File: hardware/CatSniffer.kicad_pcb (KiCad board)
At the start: 4 copper layers, 81 x 20 mm, 101 parts, among them J1 Antenna, J2 Conn_01x06_Female, J3 Conn_01x06_Female, P1 USB_C_Plug_USB2.0, SW1 SW, U1 AP2112K-3.3, U2 RFSW8006QTR7, U3 RP2040, U4 0900PC15A0036, U5 0900FM15D0039, U6 PE42421, U7 SX1262IMLTRT, U8 CC1352P1F3RGZT, U9 W25Q16JV, Y1 48MHz, Y2 32.768kHz, Y3 32Mhz, Y4 12MHz

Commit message: For revision
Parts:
- removed J2: Conn_01x06_Female, Connector:Tag-Connect_TC2030-IDC-NL_2x03_P1.27mm_Vertical
- moved R12 1.78 mm to (119.7, 109.9)
- moved G*** 1.17 mm to (130.3, 113.3)
- moved C39 0.72 mm to (116.0, 109.0), turned to 0 degrees
- moved C46 0.69 mm to (116.0, 110.0), turned to 0 degrees
- moved C28 0.54 mm to (118.4, 108.9)
- moved C4 0.49 mm to (120.3, 109.0)
- moved JP1 0.39 mm to (131.3, 103.5)
- moved C30 0.34 mm to (115.7, 107.5)
- moved G*** 0.23 mm to (132.4, 109.1)
- moved R1 0.14 mm to (94.2, 109.4)
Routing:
- net /BOOT: track 38.9 -> 92.1 mm, vias 2 -> 3
- net GND: track 382.7 -> 426.4 mm, vias 96 -> 103
- net +3V3: track 65.6 -> 98.2 mm, vias 15 -> 16
- net /RESET_SX: track 2.67 -> 28.5 mm, vias 1 -> 2
- net /cJTAG_TCK: track 17.7 -> 38.4 mm, vias 1 -> 2
- net /COPI: track 2.28 -> 22.0 mm, vias 1 -> 2
- net /CIPO: track 2.85 -> 19.8 mm, vias 1 -> 2
- net /DIO2: track 23.7 -> 38.7 mm
- net /DIO3: track 2.26 -> 15.8 mm, vias 1 -> 2
- net +1V2: track 14.3 -> 21.5 mm, vias 0 -> 3
- net /NSS: track 17.4 -> 24.4 mm
- net /RESET_CC: track 55.0 -> 62.0 mm
- net /CTF3: track 43.7 -> 48.4 mm, vias 1 -> 2
- net Net-(R12-Pad2): track 4.57 -> 6.36 mm
- net /BUSY: track 22.6 -> 24.1 mm
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- added copper zone on B.Cu, net GND
- added copper zone on F.Cu, net GND
- removed copper zone on F.Cu, net VCC

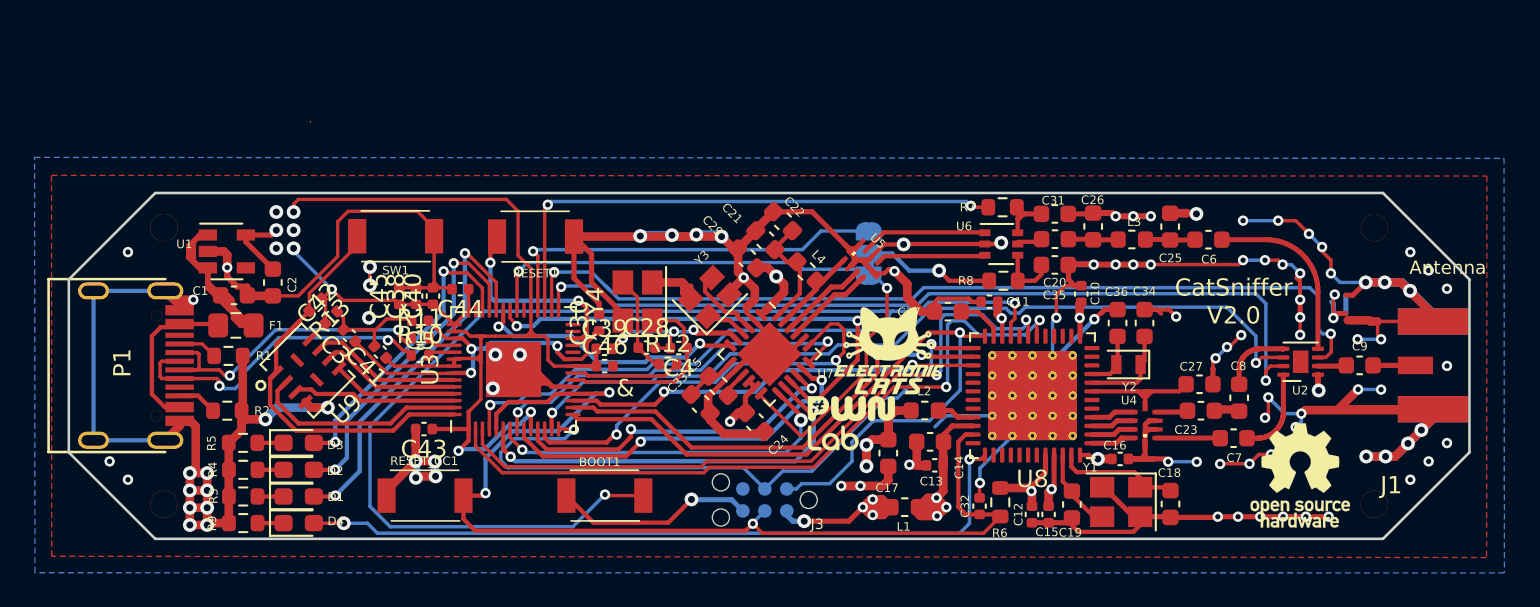
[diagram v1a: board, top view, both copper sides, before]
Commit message: schematic correction
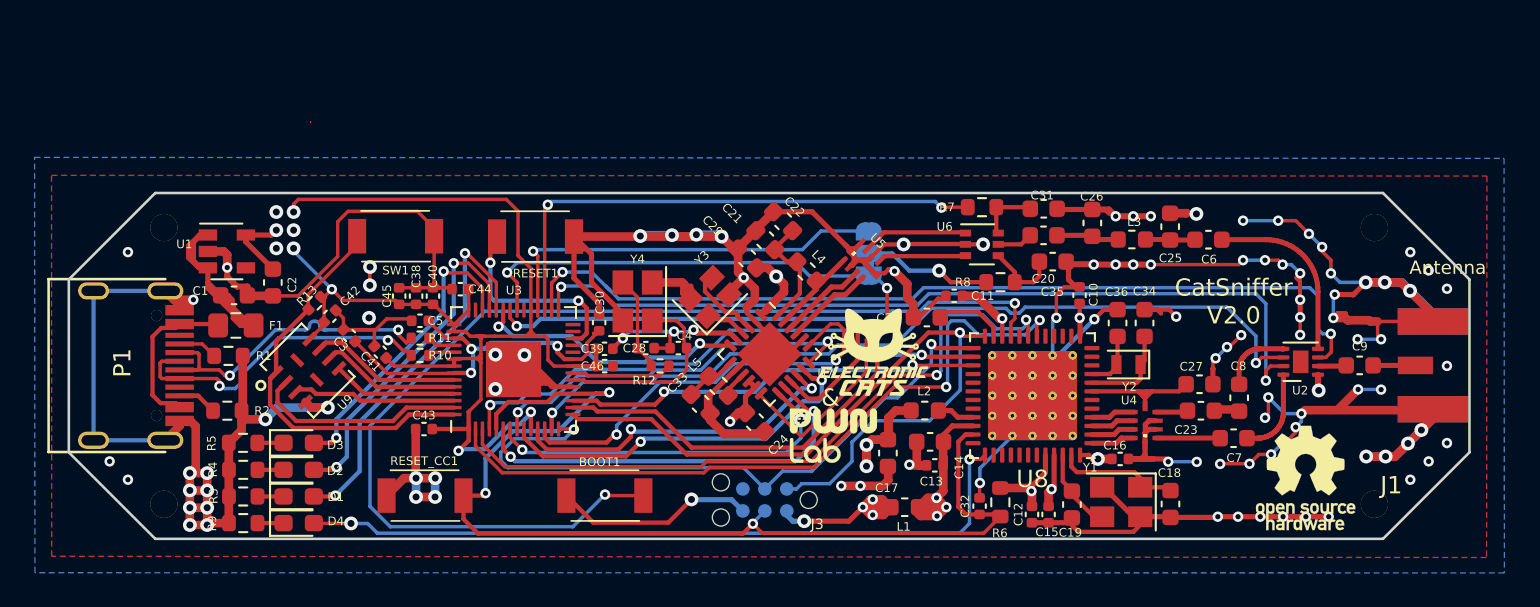
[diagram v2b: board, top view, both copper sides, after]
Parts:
- moved C11 2.07 mm to (136.2, 106.0)
- moved C37 1.27 mm to (134.6, 107.2)
- moved G*** 1.26 mm to (129.2, 114.0)
- moved R7 1.19 mm to (137.8, 100.8)
- moved U6 1.13 mm to (137.8, 103.0)
- moved G*** 0.89 mm to (131.5, 109.2)
- moved C31 0.71 mm to (141.4, 100.9)
- moved C20 0.70 mm to (141.4, 102.5)
- moved R12 0.47 mm to (119.2, 110.0)
- moved REF** 0.34 mm to (156.5, 116.5)
- moved C35 0.22 mm to (141.9, 104.0)
- moved C26 0.21 mm to (144.2, 101.7)
- moved R8 0.19 mm to (138.9, 105.2)
- moved C10 0.12 mm to (143.4, 105.9)
- moved R13 0.10 mm to (99.2, 106.4)
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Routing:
- net GND: track 426.4 -> 412.8 mm
- net VCC: track 19.6 -> 18.0 mm
- net Net-(C37-Pad1): track 2.75 -> 4.10 mm
- net /ANT_SW: track 31.9 -> 30.7 mm
- net /SW_RFI: track 6.34 -> 5.21 mm
- net /SW_RFO: track 7.32 -> 6.20 mm
- net Net-(C35-Pad1): track 3.54 -> 4.35 mm
- net Net-(C20-Pad2): track 2.91 -> 3.64 mm
- net /VDDS: track 57.9 -> 58.6 mm
- net /DIO2: track 38.7 -> 39.3 mm
- net Net-(C20-Pad1): track 1.44 -> 2.06 mm
- net /D-: track 18.4 -> 18.9 mm
- net Net-(R12-Pad2): track 6.36 -> 5.85 mm

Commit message: shcematic correction and labels
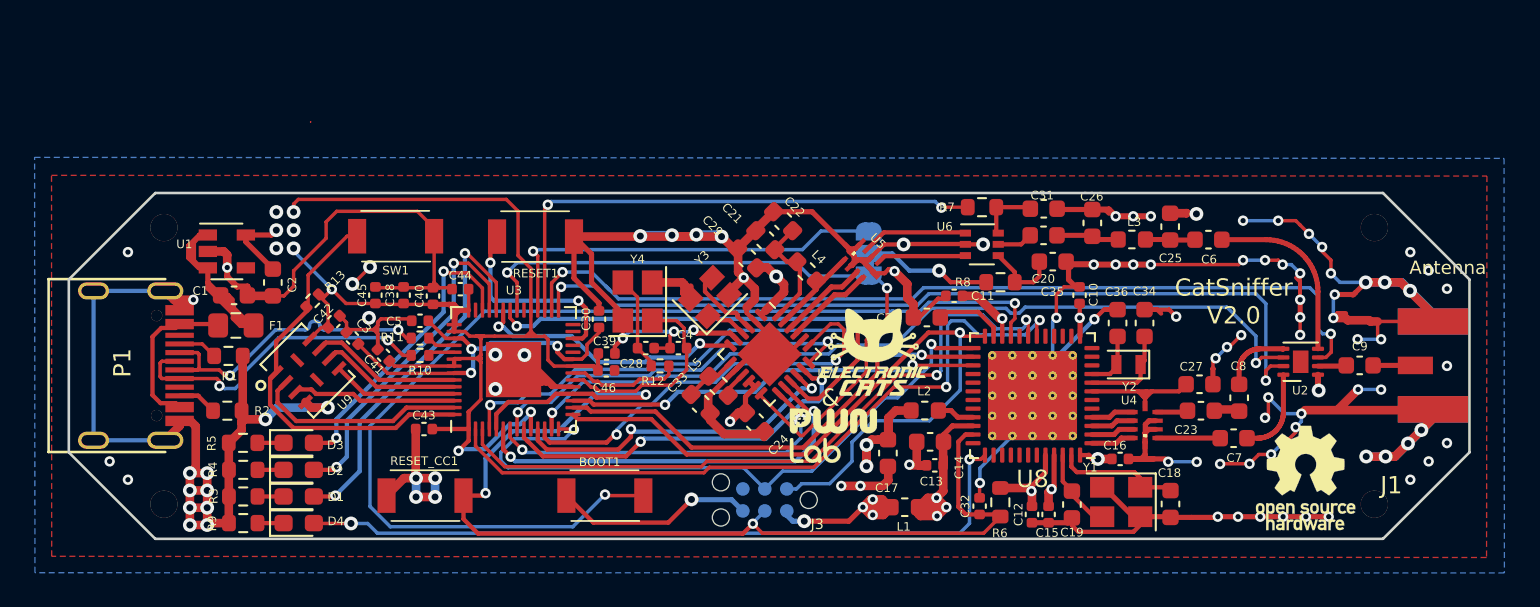
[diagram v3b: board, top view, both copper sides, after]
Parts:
- moved C45 1.37 mm to (102.7, 105.9)
- moved C38 0.72 mm to (104.4, 105.9)
- moved C42 0.39 mm to (100.3, 107.4)
- moved C39 0.30 mm to (116.1, 109.3)
- moved C46 0.27 mm to (116.1, 110.3)
- moved C41 0.26 mm to (103.2, 109.4)
- moved C3 0.23 mm to (101.4, 108.4)
- moved C30 0.19 mm to (115.7, 107.3)
- moved R13 0.18 mm to (99.1, 106.2)
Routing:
- net /RESET_CC: track 62.1 -> 66.5 mm
- net GND: track 412.8 -> 416.2 mm
- net +3V3: track 98.3 -> 100.2 mm
- net Net-(R12-Pad2): track 5.85 -> 6.58 mm

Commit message: update traces enhaced ground fix GND in. layer
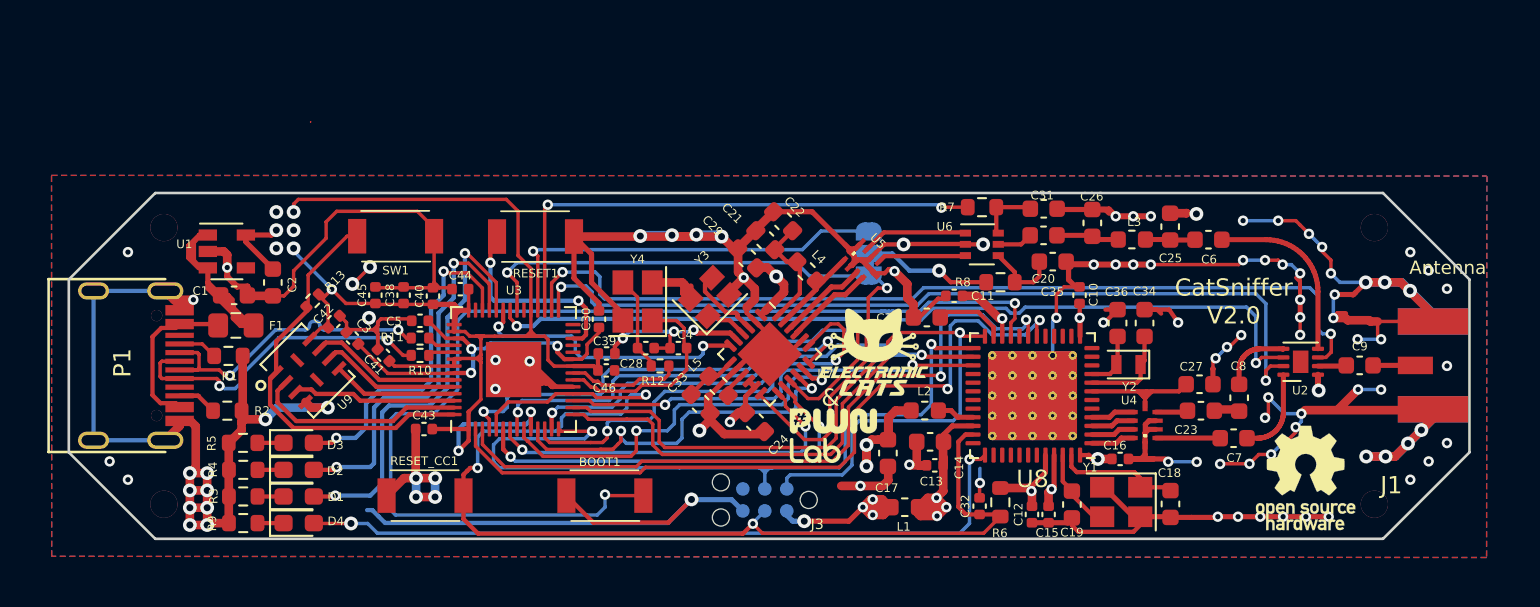
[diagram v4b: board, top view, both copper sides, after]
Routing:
- net GND: track 416.2 -> 429.1 mm
- net /cJTAG_TCK: track 38.4 -> 45.5 mm
- net /cJTAG_TMSC: track 44.2 -> 48.5 mm
- net /CIPO: track 19.8 -> 22.5 mm
- net /LED2: track 20.0 -> 22.6 mm
- net /LED3: track 22.5 -> 25.1 mm
- net /LED1: track 17.5 -> 19.6 mm
- net /CTF3: track 48.4 -> 50.3 mm
- net /BOOT: track 92.1 -> 93.9 mm
- net /JTAG/TDI: track 27.0 -> 28.5 mm
- net /TXD: track 41.7 -> 43.2 mm
- net /RXD: track 40.0 -> 41.4 mm
- net /SCK: track 22.3 -> 23.7 mm
- net /NSS: track 24.2 -> 25.6 mm
- net /DIO2: track 39.3 -> 40.6 mm
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- added copper zone on In1.Cu, net GND

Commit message: Change footprint
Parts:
- U2: footprint Package_DFN_QFN:DFN-8-1EP_2x2mm_P0.5mm_EP0.9x1.3mm -> CatSniffer:SON50P200X200X90-9N
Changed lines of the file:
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@@
       (net 1 "GND") (pinfunction "GND") (pintype "input"))
   )
-  (footprint "Package_DFN_QFN:DFN-8-1EP_2x2mm_P0.5mm_EP0.9x1.3mm" (layer "F.Cu")
+  (footprint "CatSniffer:SON50P200X200X90-9N" (layer "F.Cu")
     (at 156.24 109.76 180)
-    (descr "DFN, 8 Pin (https://www.onsemi.com/pub/Collateral/NB3N551-D.PDF#page=7), generated with kicad-footprint-generator ipc_noLead_generator.py")
-    (tags "DFN NoLead")
+    (descr "RFSW8006QTR7/")
+    (tags "Integrated Circuit")
     (property "Mouser#" "772-RFSW8006QTR7")
     (property "PARTREV" "")
@@
     (property "provedor" "Mouser")
     (attr smd)
-    (fp_text reference "U2" (at 0.03 -1.66) (layer "F.SilkS")
+    (fp_text reference "U2" (at 1 1.59 180) (layer "F.SilkS")
       (effects (font (size 0.5 0.5) (thickness 0.1)))
     )
-    (fp_text value "RFSW8006QTR7" (at 0 1.95) (layer "F.Fab")
-      (effects (font (size 1 1) (thickness 0.15)))
+    (fp_text value "RFSW8006QTR7" (at 0 0 180) (layer "F.SilkS") hide
+      (effects (font (size 1.27 1.27) (thickness 0.254)))
     )
-    (fp_text user "${REFERENCE}" (at 0 0) (layer "F.Fab")
-      (effects (font (size 0.5 0.5) (thickness 0.08)))
+    (fp_text user "${REFERENCE}" (at 0 0 180) (layer "F.Fab")
+      (effects (font (size 1.27 1.27) (thickness 0.254)))
     )
-    (fp_line (start -1 1.11) (end 1 1.11) (layer "F.SilkS") (width 0.12))
-    (fp_line (start 0 -1.11) (end 1 -1.11) (layer "F.SilkS") (width 0.12))
-    (fp_line (start -1.6 -1.25) (end -1.6 1.25) (layer "F.CrtYd") (width 0.05))
-    (fp_line (start 1.6 1.25) (end 1.6 -1.25) (layer "F.CrtYd") (width 0.05))
-    (fp_line (start -1.6 1.25) (end 1.6 1.25) (layer "F.CrtYd") (width 0.05))
-    (fp_line (start 1.6 -1.25) (end -1.6 -1.25) (layer "F.CrtYd") (width 0.05))
-    (fp_line (start -1 1) (end -1 -0.5) (layer "F.Fab") (width 0.1))
-    (fp_line (start 1 1) (end -1 1) (layer "F.Fab") (width 0.1))
-    (fp_line (start -0.5 -1) (end 1 -1) (layer "F.Fab") (width 0.1))
+    (fp_circle (center -1.35 -1.4) (end -1.35 -1.275) (layer "F.SilkS") (width 0.25) (fill none))
+    (fp_line (start -1.6 -1.275) (end 1.6 -1.275) (layer "F.CrtYd") (width 0.05))
+    (fp_line (start -1.6 1.275) (end -1.6 -1.275) (layer "F.CrtYd") (width 0.05))
+    (fp_line (start 1.6 -1.275) (end 1.6 1.275) (layer "F.CrtYd") (width 0.05))
+    (fp_line (start 1.6 1.275) (end -1.6 1.275) (layer "F.CrtYd") (width 0.05))
     (fp_line (start 1 -1) (end 1 1) (layer "F.Fab") (width 0.1))
+    (fp_line (start -1 1) (end -1 -1) (layer "F.Fab") (width 0.1))
+    (fp_line (start 1 1) (end -1 1) (layer "F.Fab") (width 0.1))
     (fp_line (start -1 -0.5) (end -0.5 -1) (layer "F.Fab") (width 0.1))
-    (pad "" smd roundrect locked (at -0.225 0.325 180) (size 0.36 0.52) (layers "F.Paste") (roundrect_rratio 0.25))
-    (pad "" smd roundrect locked (at 0.225 -0.325 180) (size 0.36 0.52) (layers "F.Paste") (roundrect_rratio 0.25))
-    (pad "" smd roundrect locked (at 0.225 0.325 180) (size 0.36 0.52) (layers "F.Paste") (roundrect_rratio 0.25))
-    (pad "" smd roundrect locked (at -0.225 -0.325 180) (size 0.36 0.52) (layers "F.Paste") (roundrect_rratio 0.25))
-    (pad "1" smd roundrect locked (at -1 -0.75 180) (size 0.7 0.25) (layers "F.Cu" "F.Paste" "F.Mask") (roundrect_rratio 0.25)
+    (fp_line (start -1 -1) (end 1 -1) (layer "F.Fab") (width 0.1))
+    (pad "1" smd rect locked (at -0.95 -0.75 270) (size 0.3 0.8) (layers "F.Cu" "F.Paste" "F.Mask")
       (net 7 "+3V3") (pinfunction "VDD") (pintype "input"))
-    (pad "2" smd roundrect locked (at -1 -0.25 180) (size 0.7 0.25) (layers "F.Cu" "F.Paste" "F.Mask") (roundrect_rratio 0.25)
+    (pad "2" smd rect locked (at -0.95 -0.25 270) (size 0.3 0.8) (layers "F.Cu" "F.Paste" "F.Mask")
       (net 6 "Net-(C9-Pad1)") (pinfunction "ANT") (pintype "input"))
-    (pad "3" smd roundrect locked (at -1 0.25 180) (size 0.7 0.25) (layers "F.Cu" "F.Paste" "F.Mask") (roundrect_rratio 0.25)
+    (pad "3" smd rect locked (at -0.95 0.25 270) (size 0.3 0.8) (layers "F.Cu" "F.Paste" "F.Mask")
       (net 39 "/CTF1") (pinfunction "CRF1") (pintype "input"))
-    (pad "4" smd roundrect locked (at -1 0.75 180) (size 0.7 0.25) (layers "F.Cu" "F.Paste" "F.Mask") (roundrect_rratio 0.25)
+    (pad "4" smd rect locked (at -0.95 0.75 270) (size 0.3 0.8) (layers "F.Cu" "F.Paste" "F.Mask")
       (net 53 "Net-(C6-Pad2)") (pinfunction "RF1") (pintype "input"))
-    (pad "5" smd roundrect locked (at 1 0.75 180) (size 0.7 0.25) (layers "F.Cu" "F.Paste" "F.Mask") (roundrect_rratio 0.25)
+    (pad "5" smd rect locked (at 0.95 0.75 270) (size 0.3 0.8) (layers "F.Cu" "F.Paste" "F.Mask")
       (net 55 "Net-(C8-Pad2)") (pinfunction "RF3") (pintype "input"))
-    (pad "6" smd roundrect locked (at 1 0.25 180) (size 0.7 0.25) (layers "F.Cu" "F.Paste" "F.Mask") (roundrect_rratio 0.25)
+    (pad "6" smd rect locked (at 0.95 0.25 270) (size 0.3 0.8) (layers "F.Cu" "F.Paste" "F.Mask")
       (net 38 "/CTF3") (pinfunction "CRF3") (pintype "input"))
-    (pad "7" smd roundrect locked (at 1 -0.25 180) (size 0.7 0.25) (layers "F.Cu" "F.Paste" "F.Mask") (roundrect_rratio 0.25)
+    (pad "7" smd rect locked (at 0.95 -0.25 270) (size 0.3 0.8) (layers "F.Cu" "F.Paste" "F.Mask")
       (net 37 "/CTF2") (pinfunction "CRF2") (pintype "input"))
-    (pad "8" smd roundrect locked (at 1 -0.75 180) (size 0.7 0.25) (layers "F.Cu" "F.Paste" "F.Mask") (roundrect_rratio 0.25)
+    (pad "8" smd rect locked (at 0.95 -0.75 270) (size 0.3 0.8) (layers "F.Cu" "F.Paste" "F.Mask")
       (net 54 "Net-(C7-Pad2)") (pinfunction "RF2") (pintype "input"))
-    (pad "9" smd rect locked (at 0 0 180) (size 0.9 1.3) (layers "F.Cu" "F.Mask"))
-    (model "${KISYS3DMOD}/Package_DFN_QFN.3dshapes/DFN-8-1EP_2x2mm_P0.5mm_EP0.9x1.3mm.wrl"
+    (pad "9" smd rect locked (at 0 0 180) (size 0.65 1.25) (layers "F.Cu" "F.Paste" "F.Mask"))
+    (model "RFSW8006QTR7.stp"
       (offset (xyz 0 0 0))
       (scale (xyz 1 1 1))
@@
   (segment (start 108.12 106.78) (end 107.61 106.78) (width 0.3) (layer "F.Cu") (net 7))
   (segment (start 112.01 108.28) (end 112.52 108.28) (width 0.2) (layer "F.Cu") (net 7))
-  (segment (start 157.24 111.38) (end 157.28 111.42) (width 0.35) (layer "F.Cu") (net 7))
   (segment (start 107.61 106.78) (end 107.34 107.05) (width 0.3) (layer "F.Cu") (net 7))
   (segment (start 124.575405 111.123122) (end 124.327926 110.875643) (width 0.3) (layer "F.Cu") (net 7))
@@
   (segment (start 131.49 118.62) (end 132.105 118.62) (width 0.5) (layer "F.Cu") (net 7))
   (segment (start 132.49 118.17) (end 132.04 117.72) (width 0.5) (layer "F.Cu") (net 7))
+  (segment (start 157.24 111.6) (end 157.24 110.51) (width 0.35) (layer "F.Cu") (net 7))
   (segment (start 108.61 109.57) (end 108.83 109.35) (width 0.2) (layer "F.Cu") (net 7))
   (segment (start 109.01 108.28) (end 109.622182 108.28) (width 0.2) (layer "F.Cu") (net 7))
@@
   (segment (start 107.2825 106.7225) (end 107.2825 107.61) (width 0.3) (layer "F.Cu") (net 7))
   (segment (start 124.131992 112.701992) (end 123.728008 112.701992) (width 0.5) (layer "F.Cu") (net 7))
-  (segment (start 157.24 110.51) (end 157.24 111.38) (width 0.35) (layer "F.Cu") (net 7))
   (segment (start 111.5 108.26) (end 111.68 108.26) (width 0.2) (layer "F.Cu") (net 7))
   (segment (start 125.395022 104.31) (end 125.91 104.824978) (width 0.5) (layer "F.Cu") (net 7))
@@
   (via (at 98 103.2) (size 0.8) (drill 0.4) (layers "F.Cu" "B.Cu") (net 7))
   (via (at 97 103.2) (size 0.8) (drill 0.4) (layers "F.Cu" "B.Cu") (net 7))
-  (via (at 157.28 111.42) (size 0.8) (drill 0.4) (layers "F.Cu" "B.Cu") (net 7))
+  (via (at 157.24 111.6) (size 0.8) (drill 0.4) (layers "F.Cu" "B.Cu") (net 7))
   (via (at 100.21 105.57) (size 0.6) (drill 0.3) (layers "F.Cu" "B.Cu") (net 7))
   (via (at 97 101.1) (size 0.8) (drill 0.4) (layers "F.Cu" "B.Cu") (net 7))

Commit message: Edit silkscreen
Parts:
- moved G*** 1.41 mm to (128.7, 115.4)
- moved G*** 0.33 mm to (131.6, 109.5)
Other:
- board text added: "CatSniffer V3.0"
- board text added: "CatSniffer v3.0"
- board text removed: "CatSniffer V2.0"
- board text removed: "CatSniffer v2.0"
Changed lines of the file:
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@@
     (property "provedor" "Mouser")
     (attr smd)
-    (fp_text reference "U7" (at 3.090057 -1.477853) (layer "F.SilkS")
+    (fp_text reference "U7" (at 0.247487 8.039804) (layer "F.SilkS")
       (effects (font (size 0.5 0.5) (thickness 0.1)))
     )
@@
     (property "provedor" "Mouser")
     (attr smd)
-    (fp_text reference "L2" (at 0.03 1.11) (layer "F.SilkS")
+    (fp_text reference "L2" (at 0.01 1.06) (layer "F.SilkS")
       (effects (font (size 0.5 0.5) (thickness 0.1)))
     )
@@
     (property "provedor" "LCSC")
     (attr smd)
-    (fp_text reference "C37" (at 2.25 -0.03) (layer "F.SilkS")
+    (fp_text reference "C37" (at -0.01 -1.11) (layer "F.SilkS")
       (effects (font (size 0.5 0.5) (thickness 0.12)))
     )
@@
   )
   (footprint "Aesthetics:electronic_cats_logo_4x3" (layer "F.Cu")
-    (at 131.53 109.21)
+    (at 131.61 109.53)
     (attr through_hole)
     (fp_text reference "G***" (at 0 0) (layer "F.SilkS") hide
@@
     (property "provedor" "LCSC")
     (attr smd)
-    (fp_text reference "C24" (at 1.887975 -0.021213 225) (layer "F.SilkS")
+    (fp_text reference "C24" (at 0.035355 1.053589 135) (layer "F.SilkS")
       (effects (font (size 0.5 0.5) (thickness 0.1)))
     )
@@
   )
   (footprint "CatSniffer:calderon" (layer "F.Cu")
-    (at 129.22 114.04)
+    (at 128.73 115.36)
     (attr through_hole)
     (fp_text reference "G***" (at 0 0) (layer "F.SilkS") hide
@@
   (gr_line (start 90 120) (end 161 120) (layer "Edge.Cuts") (width 0.15))
   (gr_line (start 85 105) (end 85 115) (layer "Edge.Cuts") (width 0.15))
-  (gr_text "CatSniffer\nv2.0" (at 98.298 110.236) (layer "B.SilkS")
+  (gr_text "CatSniffer\nv3.0" (at 98.298 110.236) (layer "B.SilkS")
     (effects (font (size 1.5 1.5) (thickness 0.25)) (justify mirror))
   )
@@
     (effects (font (size 1 1) (thickness 0.15)) (justify mirror))
   )
-  (gr_text "&" (at 129.05 111.84) (layer "F.SilkS")
+  (gr_text "&" (at 130.56 113) (layer "F.SilkS")
     (effects (font (size 1 1) (thickness 0.15)))
   )
-  (gr_text "CatSniffer\nV2.0" (at 152.37 106.28) (layer "F.SilkS")
+  (gr_text "CatSniffer\nV3.0" (at 152.37 106.28) (layer "F.SilkS")
     (effects (font (size 1 1) (thickness 0.15)))
   )
